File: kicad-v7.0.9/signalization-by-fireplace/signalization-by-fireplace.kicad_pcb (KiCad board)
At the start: 2 copper layers, 129.8 x 92.5 mm, 115 parts, among them J1 2x1x4_idc_lsa, J2 EBBA-03-C-SS-BU, J3 54601-908WPLF, J4 2x1x4_idc_lsa, J5 DG390-5.0, J6 EBBA-02-C-SS-BU, P1 DS1023-1-4S21, P10 DS1021-1-2SF11-B, P11 DS1021-1-2SF11-B, P12 DS1021-1-3SF11-B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

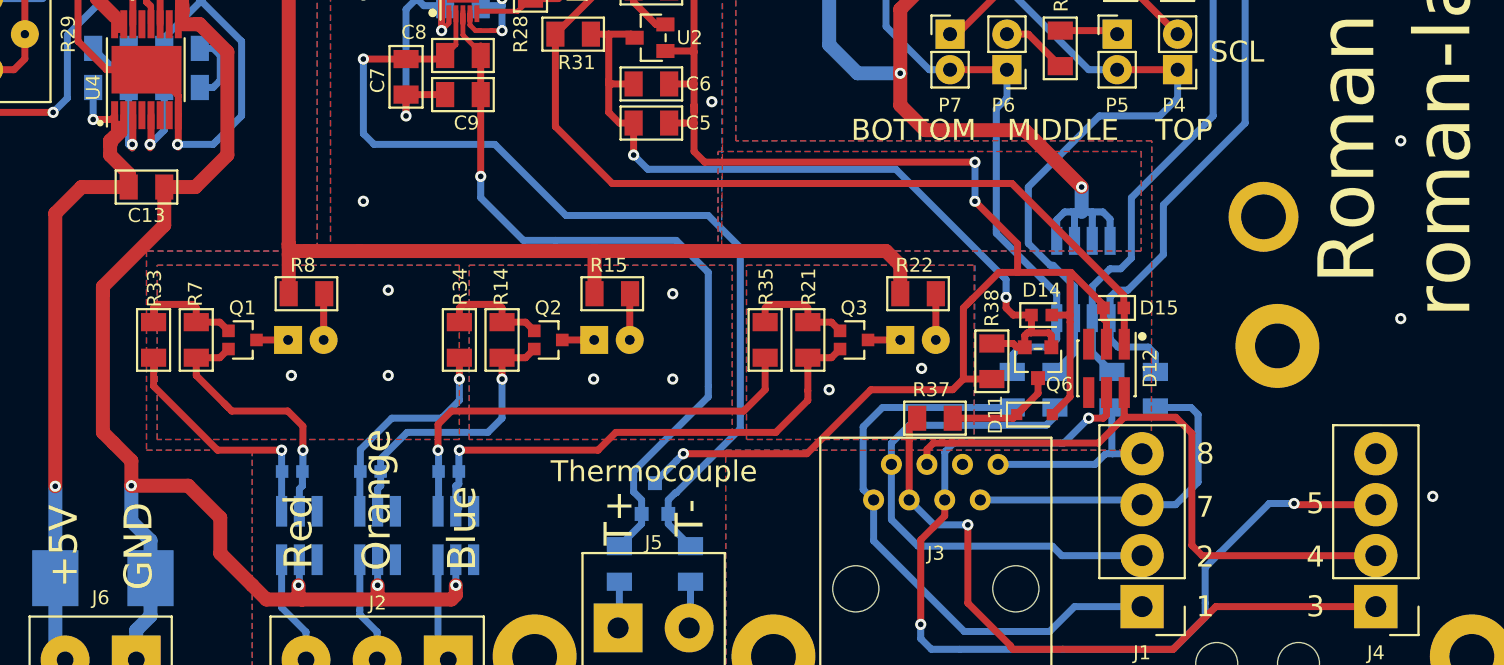
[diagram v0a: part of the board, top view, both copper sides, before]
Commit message: Change of components from edited library. Change folder structure.
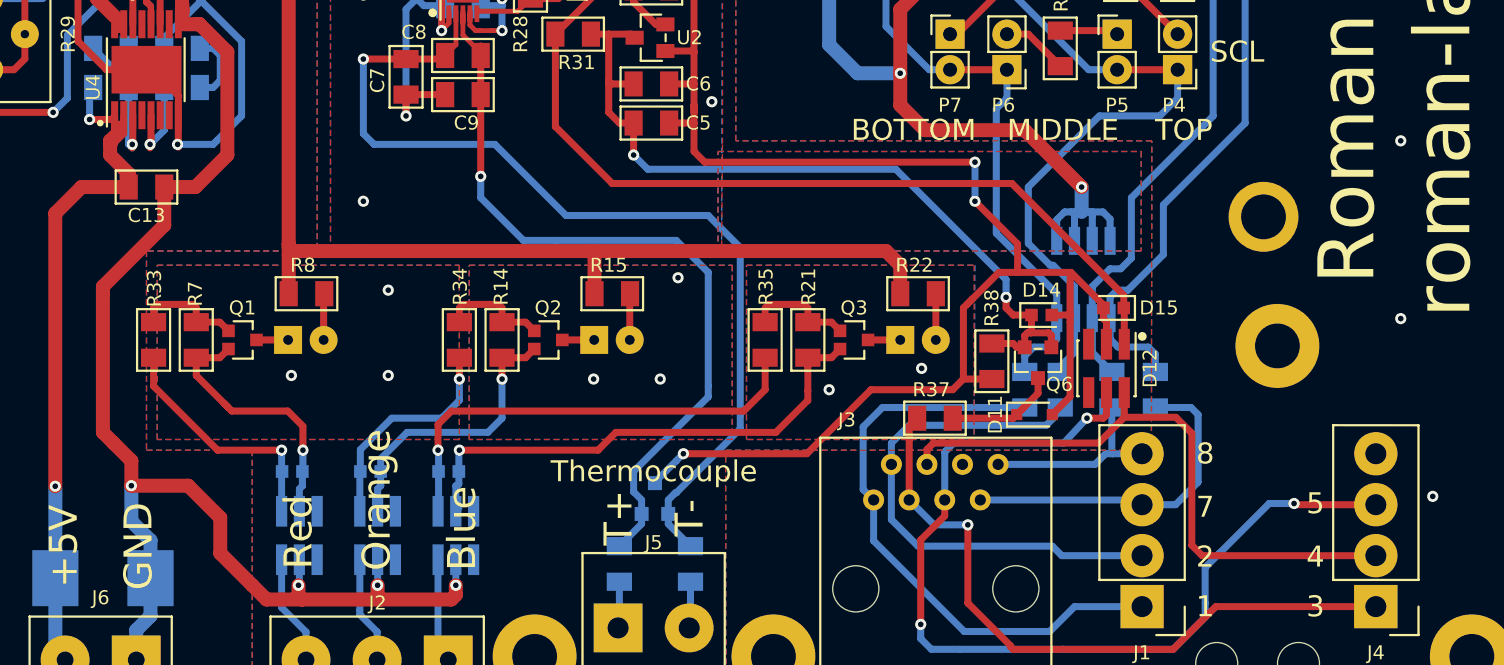
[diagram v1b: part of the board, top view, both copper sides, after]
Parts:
- J3: footprint connector_rl:rj45_54601-908WPLF -> connector_rj45_tht_rl:54601-908WPLF
- moved R4 0.89 mm to (176.8, 119.0)
- moved R3 0.38 mm to (179.4, 119.0)
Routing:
- net /DSCL_N: track 46.3 -> 45.4 mm

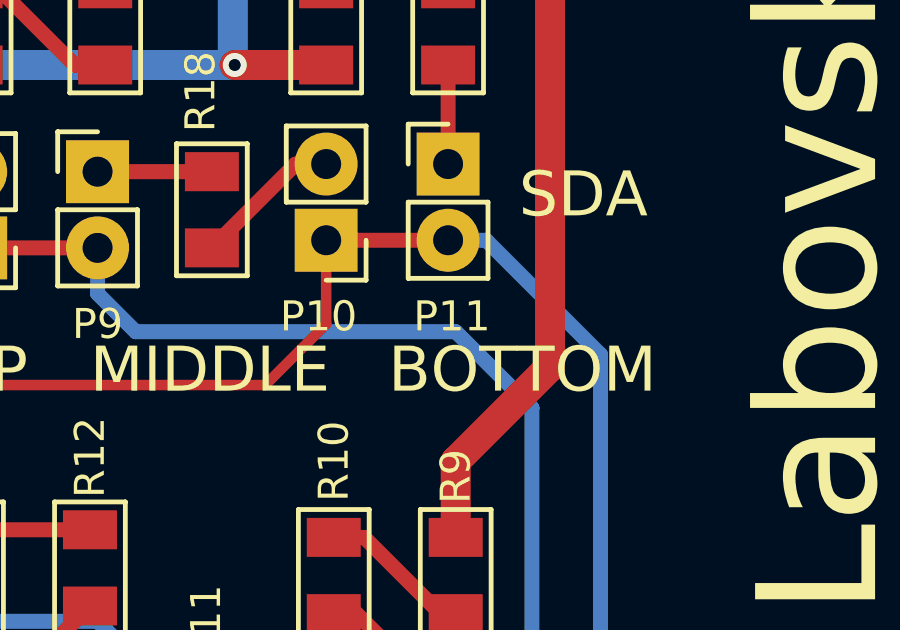
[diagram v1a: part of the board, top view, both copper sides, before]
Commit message: Change components form library. Adding of BOM.
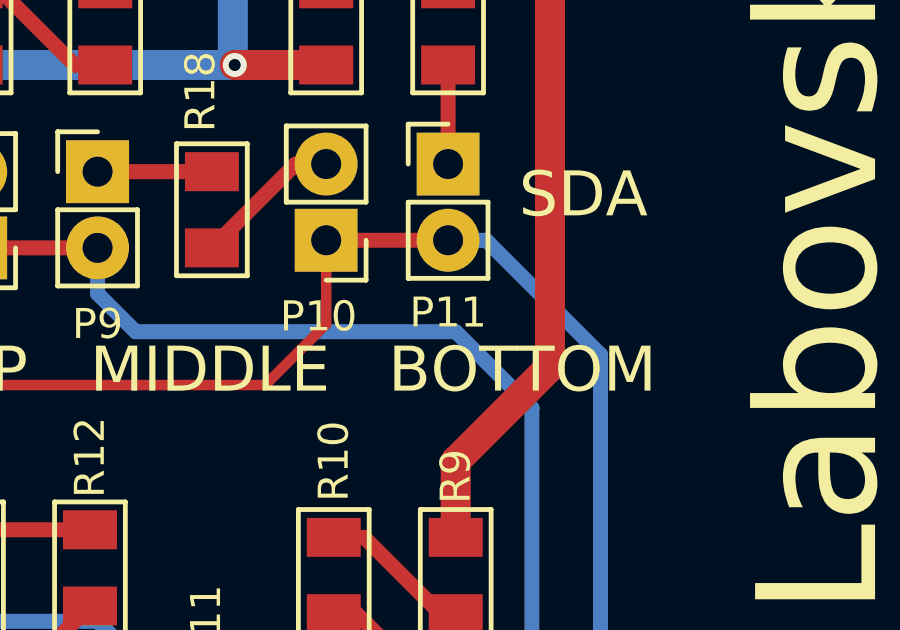
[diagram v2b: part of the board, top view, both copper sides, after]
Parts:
- J1, J4: footprint connector_rl:1x4_idc_lsa_connector_general -> connector_idc_lsa_tht_rl:1x4_idc_lsa_connector_general
- P1: footprint connector_tht_pinsocket_2.54mm_rl:1x4_pinsocket_2.54mm_vertical_8.4mm -> connector_pin_socket_2.54mm_tht_rl:1x4_pin_socket_2.54mm_vertical_8.5mm
- P10, P11, P2, P3, P4, P5, P6, P7, P8, P9: footprint connector_tht_pinheader_2.54mm_rl:1x2_pinheader_2.54mm_vertical -> connector_pin_header_2.54mm_tht_rl:1x2_pin_header_2.54mm_vertical
- P12, P13, P14, P15: footprint connector_tht_pinheader_2.54mm_rl:1x3_pinheader_2.54mm_vertical -> connector_pin_header_2.54mm_tht_rl:1x3_pin_header_2.54mm_vertical
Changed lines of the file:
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@@
     )
   )
-  (footprint "connector_tht_pinheader_2.54mm_rl:1x2_pinheader_2.54mm_vertical" (layer "F.Cu")
+  (footprint "connector_pin_header_2.54mm_tht_rl:1x2_pin_header_2.54mm_vertical" (layer "F.Cu")
     (at 159.5755 74.549 180)
     (descr "Through hole straight pin header, 1x2, 2.54mm pitch, single row")
@@
     )
   )
-  (footprint "connector_tht_pinheader_2.54mm_rl:1x2_pinheader_2.54mm_vertical" (layer "F.Cu")
+  (footprint "connector_pin_header_2.54mm_tht_rl:1x2_pin_header_2.54mm_vertical" (layer "F.Cu")
     (at 187.7695 96.139 180)
     (descr "Through hole straight pin header, 1x2, 2.54mm pitch, single row")
@@
     )
   )
-  (footprint "connector_tht_pinheader_2.54mm_rl:1x2_pinheader_2.54mm_vertical" (layer "F.Cu")
+  (footprint "connector_pin_header_2.54mm_tht_rl:1x2_pin_header_2.54mm_vertical" (layer "F.Cu")
     (at 183.4515 93.599)
     (descr "Through hole straight pin header, 1x2, 2.54mm pitch, single row")
@@
     )
   )
-  (footprint "connector_tht_pinheader_2.54mm_rl:1x2_pinheader_2.54mm_vertical" (layer "F.Cu")
+  (footprint "connector_pin_header_2.54mm_tht_rl:1x2_pin_header_2.54mm_vertical" (layer "F.Cu")
     (at 175.5775 96.139 180)
     (descr "Through hole straight pin header, 1x2, 2.54mm pitch, single row")
@@
     )
   )
-  (footprint "connector_tht_pinheader_2.54mm_rl:1x2_pinheader_2.54mm_vertical" (layer "F.Cu")
+  (footprint "connector_pin_header_2.54mm_tht_rl:1x2_pin_header_2.54mm_vertical" (layer "F.Cu")
     (at 171.5135 93.599)
     (descr "Through hole straight pin header, 1x2, 2.54mm pitch, single row")
@@
     )
   )
-  (footprint "connector_tht_pinheader_2.54mm_rl:1x2_pinheader_2.54mm_vertical" (layer "F.Cu")
+  (footprint "connector_pin_header_2.54mm_tht_rl:1x2_pin_header_2.54mm_vertical" (layer "F.Cu")
     (at 171.7675 78.105 180)
     (descr "Through hole straight pin header, 1x2, 2.54mm pitch, single row")
@@
     )
   )
-  (footprint "connector_tht_pinheader_2.54mm_rl:1x2_pinheader_2.54mm_vertical" (layer "F.Cu")
+  (footprint "connector_pin_header_2.54mm_tht_rl:1x2_pin_header_2.54mm_vertical" (layer "F.Cu")
     (at 175.8315 75.565)
     (descr "Through hole straight pin header, 1x2, 2.54mm pitch, single row")
@@
     )
   )
-  (footprint "connector_tht_pinheader_2.54mm_rl:1x2_pinheader_2.54mm_vertical" (layer "F.Cu")
+  (footprint "connector_pin_header_2.54mm_tht_rl:1x2_pin_header_2.54mm_vertical" (layer "F.Cu")
     (at 183.4515 77.851 180)
     (descr "Through hole straight pin header, 1x2, 2.54mm pitch, single row")
@@
     )
   )
-  (footprint "connector_tht_pinheader_2.54mm_rl:1x2_pinheader_2.54mm_vertical" (layer "F.Cu")
+  (footprint "connector_pin_header_2.54mm_tht_rl:1x2_pin_header_2.54mm_vertical" (layer "F.Cu")
     (at 187.5155 75.311)
     (descr "Through hole straight pin header, 1x2, 2.54mm pitch, single row")
@@
     (property "ki_keywords" "1x2 header pins")
     (attr through_hole)
-    (fp_text reference "P11" (at 0.127 5.08) (layer "F.SilkS")
+    (fp_text reference "P11" (at 0 4.953) (layer "F.SilkS")
         (effects (font (size 1 1) (thickness 0.16)))
     )
@@
     )
   )
-  (footprint "connector_tht_pinheader_2.54mm_rl:1x3_pinheader_2.54mm_vertical" (layer "F.Cu")
+  (footprint "connector_pin_header_2.54mm_tht_rl:1x3_pin_header_2.54mm_vertical" (layer "F.Cu")
     (at 143.5735 82.423 180)
     (descr "Through hole straight pin header, 1x3, 2.54mm pitch, single row")
@@
     )
   )
-  (footprint "connector_tht_pinheader_2.54mm_rl:1x3_pinheader_2.54mm_vertical" (layer "F.Cu")
+  (footprint "connector_pin_header_2.54mm_tht_rl:1x3_pin_header_2.54mm_vertical" (layer "F.Cu")
     (at 139.0015 82.423 180)
     (descr "Through hole straight pin header, 1x3, 2.54mm pitch, single row")
@@
     )
   )
-  (footprint "connector_tht_pinheader_2.54mm_rl:1x3_pinheader_2.54mm_vertical" (layer "F.Cu")
+  (footprint "connector_pin_header_2.54mm_tht_rl:1x3_pin_header_2.54mm_vertical" (layer "F.Cu")
     (at 134.4295 82.423 180)
     (descr "Through hole straight pin header, 1x3, 2.54mm pitch, single row")
@@
     )
   )
-  (footprint "connector_tht_pinheader_2.54mm_rl:1x3_pinheader_2.54mm_vertical" (layer "F.Cu")
+  (footprint "connector_pin_header_2.54mm_tht_rl:1x3_pin_header_2.54mm_vertical" (layer "F.Cu")
     (at 129.8575 82.423 180)
     (descr "Through hole straight pin header, 1x3, 2.54mm pitch, single row")
@@
     (property "ki_description" "Cold-Junction compensated 1-Wire thermocouple to digital converter")
     (property "ki_keywords" "thermocouple  converter max31850k")
-    (attr through_hole)
+    (attr smd)
     (fp_text reference "U3" (at 0 -2.54 90) (layer "F.SilkS")
         (effects (font (size 1 1) (thickness 0.16)))
@@
     )
   )
-  (footprint "connector_tht_pinheader_2.54mm_rl:1x2_pinheader_2.54mm_vertical" (layer "F.Cu")
+  (footprint "connector_pin_header_2.54mm_tht_rl:1x2_pin_header_2.54mm_vertical" (layer "F.Cu")
     (at 153.7335 74.549 180)
     (descr "Through hole straight pin header, 1x2, 2.54mm pitch, single row")
@@
     )
   )
-  (footprint "connector_rl:1x4_idc_lsa_connector_general" (layer "F.Cu")
+  (footprint "connector_idc_lsa_tht_rl:1x4_idc_lsa_connector_general" (layer "F.Cu")
     (at 201.93 134.493 180)
     (descr "General IDC/LSA connector")
@@
     )
   )
-  (footprint "connector_rl:1x4_idc_lsa_connector_general" (layer "F.Cu")
+  (footprint "connector_idc_lsa_tht_rl:1x4_idc_lsa_connector_general" (layer "F.Cu")
     (at 185.2295 134.493 180)
     (descr "General IDC/LSA connector")
@@
     )
   )
-  (footprint "connector_tht_pinsocket_2.54mm_rl:1x4_pinsocket_2.54mm_vertical_8.4mm" (layer "B.Cu")
+  (footprint "connector_pin_socket_2.54mm_tht_rl:1x4_pin_socket_2.54mm_vertical_8.5mm" (layer "B.Cu")
     (at 187.0127 63.22874)
-    (descr "1x4 pin socket, spacing 2.54 mm, vertical, vertical 8.4 mm")
-    (tags "1x4 pin socket 8.4 mm")
+    (descr "1x4 pin socket, spacing 2.54 mm, vertical, vertical 8.5 mm")
+    (tags "1x4 pin socket 8.5 mm")
     (property "Sheetfile" "signalization-by-fireplace.kicad_sch")
     (property "Sheetname" "")
-    (property "ki_description" "1x4 pin socket. Height 8.4 mm.")
+    (property "ki_description" "1x4 pin socket. Height 8.5 mm.")
     (property "ki_keywords" "1x4 socket")
     (attr through_hole)
@@
     (pad "4" thru_hole oval (at 0 -7.62) (size 2.1 2.1) (drill 1) (layers "*.Cu" "*.Mask")
       (net 1 "GND") (pinfunction "4") (pintype "passive"))
-    (model "${KICAD_3DPACKAGE_DIR_RL}/connector_pinsocket_2.54mm.3dshapes/tht/1x4_pinsocket_2.54mm_vertical_8.4mm.step"
-      (offset (xyz 0 -11.45 0))
+    (model "${KICAD_3DPACKAGE_DIR_RL}/connector_pinsocket_2.54mm.3dshapes/tht/1x4_pinsocket_2.54mm_vertical_8.5mm.step"
+      (offset (xyz 0 0 0))
       (scale (xyz 1 1 1))
-      (rotate (xyz 0 0 0))
+      (rotate (xyz -90 0 90))
     )
   )
